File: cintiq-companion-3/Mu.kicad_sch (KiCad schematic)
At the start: 12 parts, among them J1 Conn_01x03_Pin

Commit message: updated notes
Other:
- note added: "rough HSIO plan: HSIO A: USB3, 2nd E-key PCIe x1 link and B-key PCIe x2/USB3 link 0: USB 3.2 Type-A 1: Wifi PCIe x1 link 2 2: B-key x2 Lane 1 / USB3.2 3: B-key x2 Lane 0 HSIO B: PCIe 4x1, HSIO11 sata/pcie with gpio for M-key m.2 slot 8: SSD PCIe x4 Lane 3 9: SSD PCIe x4 Lane 2 10: SSD PCIe x4 Lane 1 (/ SATA?) 11: SSD PCIe x4 Lane 0 / SATA HSIO C: PCIe 1x1 for E-key m.2 slot for Wifi 6: Wifi PCIe 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"
- note removed: "rough HSIO plan: HSIO A: USB3, 2nd E-key PCIe x1 link and B-key PCIe x2/USB3 link 0: USB 3.2 Type-A 1: Wifi PCIe x1 link 2 2: B-key x2 Lane 1/USB3.2 3: B-key x2 Lane 0 HSIO B: PCIe 4x1, HSIO11 sata/pcie with gpio for M-key m.2 slot 8: SSD PCIe x4 Lane 3 9: SSD PCIe x4 Lane 2 10: SSD PCIe x4 Lane 1 (/ SATA?) 11: SSD PCIe x4 Lane 0 / SATA HSIO C: PCIe 1x1 for E-key m.2 slot for Wifi 6: Wifi PCIe x1"
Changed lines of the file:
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@@
 		)
 	)
-	(text_box "USB2 P3/P4 used for 13HD stuff?"
-		(exclude_from_sim no)
-		(at 265.43 203.2 0)
-		(size 39.37 13.97)
+	(text_box "USB2 P3/P4 used for M.2 slots"
+		(exclude_from_sim no)
+		(at 264.16 198.12 0)
+		(size 40.64 10.16)
 		(stroke
 			(width 0)
@@
 		)
 	)
-	(text_box "USB2 P1/P2 used for USB3.0?"
-		(exclude_from_sim no)
-		(at 265.43 193.04 0)
-		(size 39.37 10.16)
+	(text_box "USB2 P1/P2 used for 13HD stuff"
+		(exclude_from_sim no)
+		(at 264.16 187.96 0)
+		(size 40.64 10.16)
+		(stroke
+			(width 0)
+			(type default)
+		)
+		(fill
+			(type none)
+		)
+		(effects
+			(font
+				(size 2.54 2.54)
+				(thickness 0.508)
+				(bold yes)
+				(color 255 121 154 1)
+			)
+			(justify left top)
+		)
+	)
+	(text_box "USB2 P7/P8 used for type-c + ?"
+		(exclude_from_sim no)
+		(at 264.16 208.28 0)
+		(size 40.64 10.16)
 		(stroke
 			(width 0)
@@
 		)
 	)
-	(text "rough HSIO plan:\n\nHSIO A:\nUSB3, 2nd E-key PCIe x1 link and B-key PCIe x2/USB3 link\n0:  USB 3.2 Type-A\n1:  Wifi PCIe x1 link 2\n2:  B-key x2 Lane 1/USB3.2\n3:  B-key x2 Lane 0\n\nHSIO B:\nPCIe 4x1, HSIO11 sata/pcie with gpio for M-key m.2 slot\n8:  SSD PCIe x4 Lane 3\n9:  SSD PCIe x4 Lane 2\n10: SSD PCIe x4 Lane 1 (/ SATA?)\n11: SSD PCIe x4 Lane 0 / SATA\n\nHSIO C:\nPCIe 1x1 for E-key m.2 slot for Wifi\n6:  Wifi PCIe x1 "
+	(text "rough HSIO plan:\n\nHSIO A:\nUSB3, 2nd E-key PCIe x1 link and B-key PCIe x2/USB3 link\n0:  USB 3.2 Type-A\n1:  Wifi PCIe x1 link 2\n2:  B-key x2 Lane 1 / USB3.2\n3:  B-key x2 Lane 0\n\nHSIO B:\nPCIe 4x1, HSIO11 sata/pcie with gpio for M-key m.2 slot\n8:  SSD PCIe x4 Lane 3\n9:  SSD PCIe x4 Lane 2\n10: SSD PCIe x4 Lane 1 (/ SATA?)\n11: SSD PCIe x4 Lane 0 / SATA\n\nHSIO C:\nPCIe 1x1 for E-key m.2 slot for Wifi\n6:  Wifi PCIe x1 "
 		(exclude_from_sim no)
 		(at 127 123.19 0)

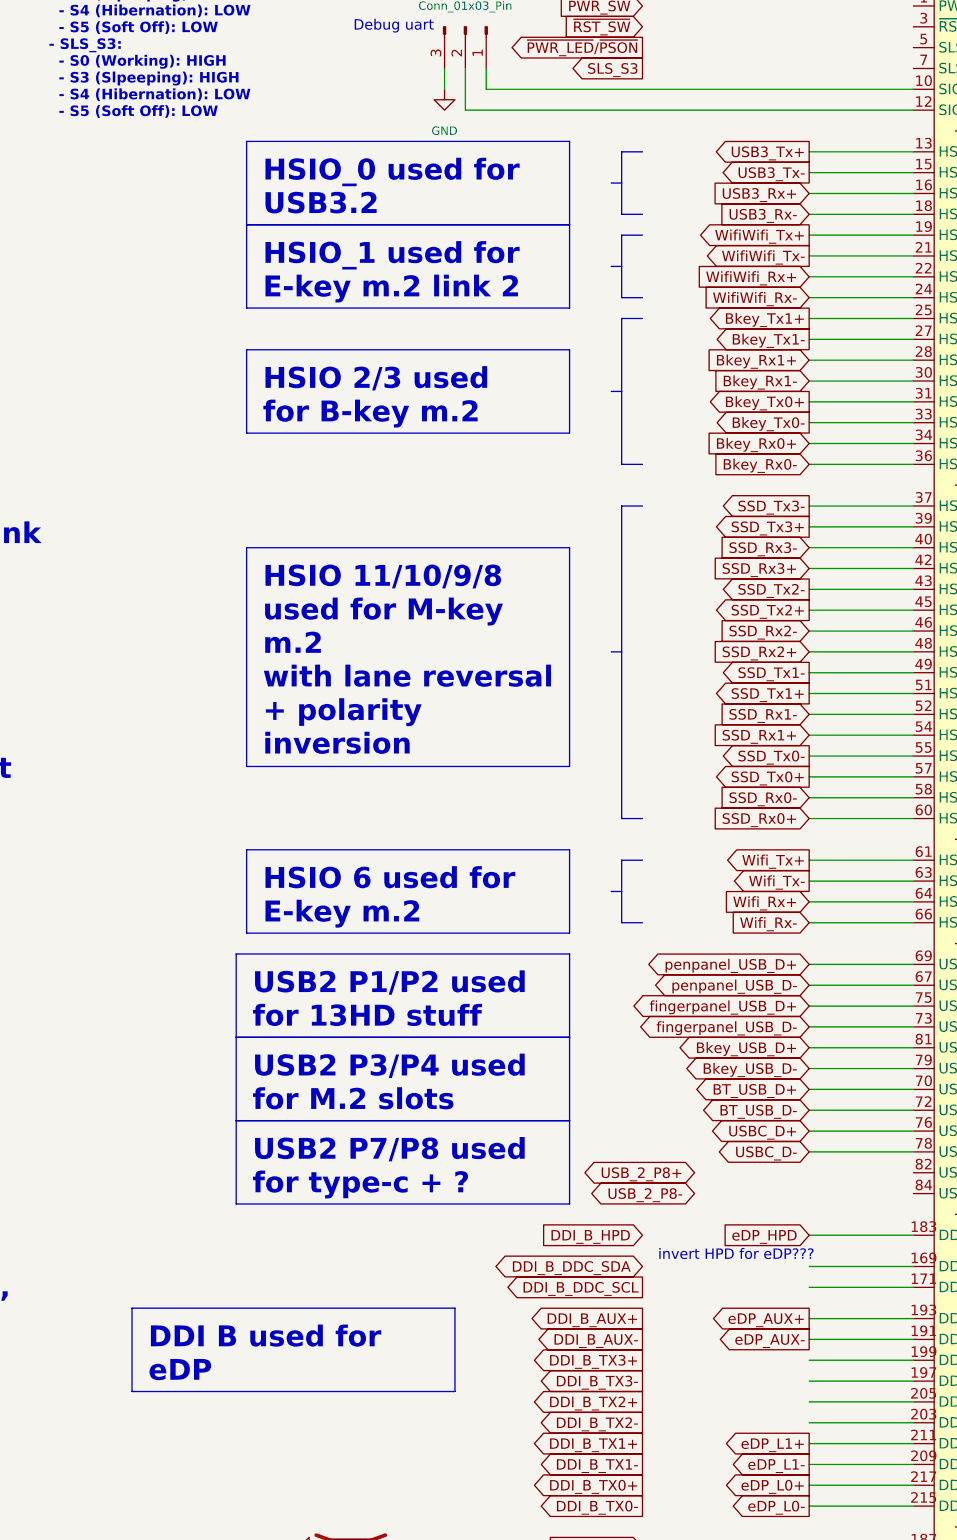
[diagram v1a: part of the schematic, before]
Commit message: unflipped m-key polarity for sata
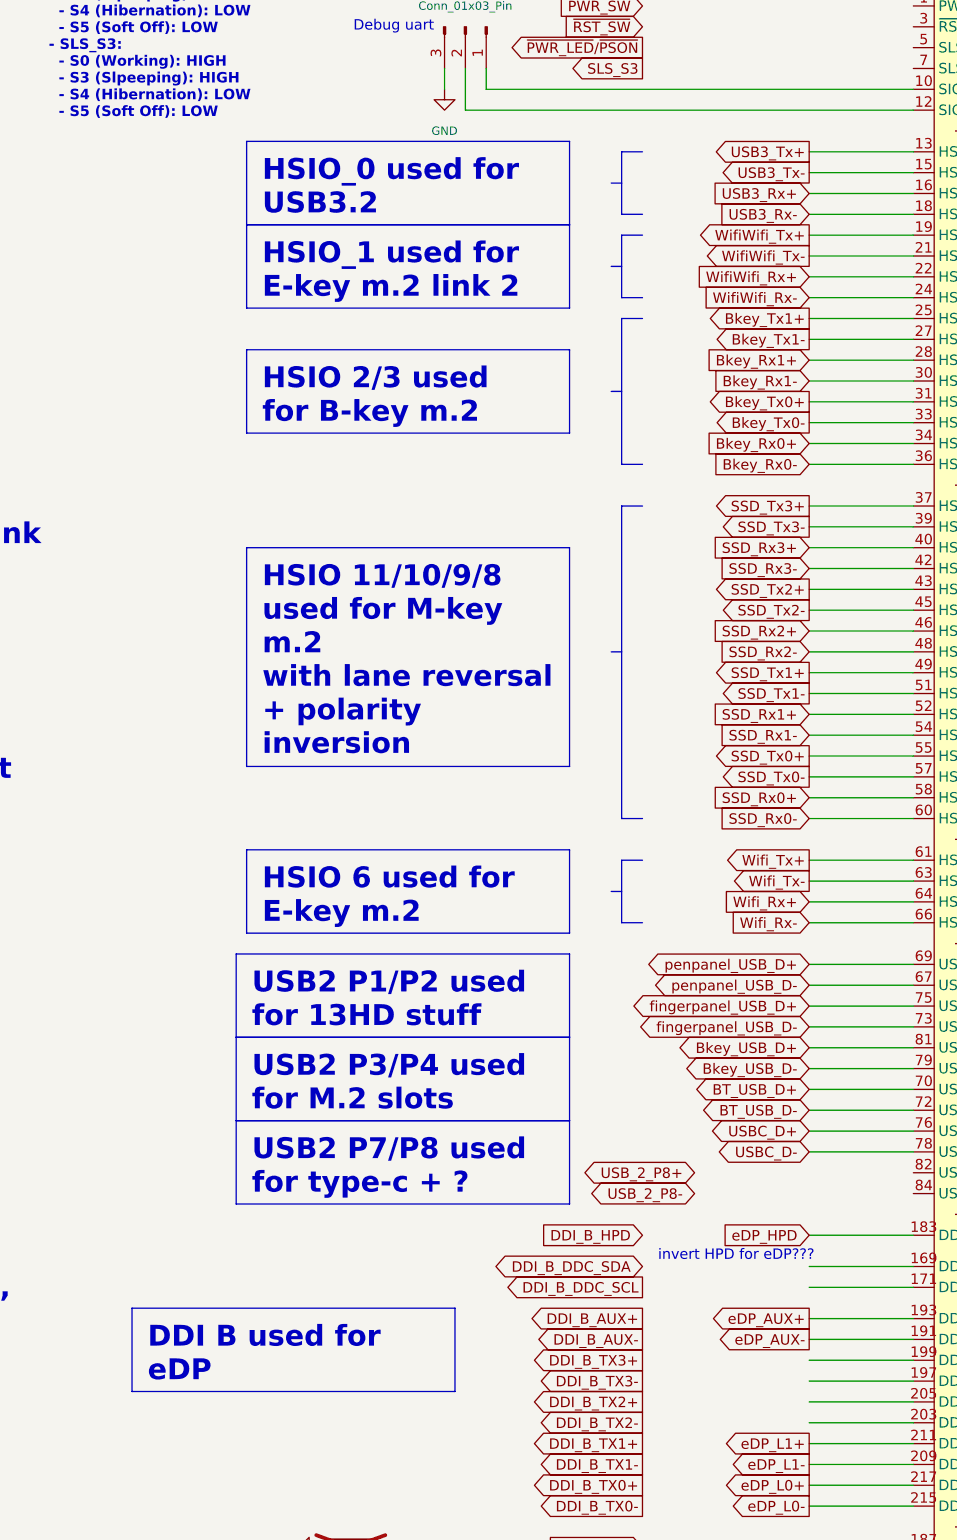
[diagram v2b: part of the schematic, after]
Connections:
- net SSD_Rx0+: now also A1.58 (HSIO11_RX+); no longer A1.60 (HSIO11_RX-)
- net SSD_Rx0-: now also A1.60 (HSIO11_RX-); no longer A1.58 (HSIO11_RX+)
- net SSD_Rx1+: now also A1.52 (HSIO10_RX+); no longer A1.54 (HSIO10_RX-)
- net SSD_Rx1-: now also A1.54 (HSIO10_RX-); no longer A1.52 (HSIO10_RX+)
- net SSD_Rx2+: now also A1.46 (HSIO9_RX+); no longer A1.48 (HSIO9_RX-)
- net SSD_Rx2-: now also A1.48 (HSIO9_RX-); no longer A1.46 (HSIO9_RX+)
- net SSD_Rx3+: now also A1.40 (HSIO8_RX+); no longer A1.42 (HSIO8_RX-)
- net SSD_Rx3-: now also A1.42 (HSIO8_RX-); no longer A1.40 (HSIO8_RX+)
- net SSD_Tx0+: now also A1.55 (HSIO11_TX+); no longer A1.57 (HSIO11_TX-)
- net SSD_Tx0-: now also A1.57 (HSIO11_TX-); no longer A1.55 (HSIO11_TX+)
- net SSD_Tx1+: now also A1.49 (HSIO10_TX+); no longer A1.51 (HSIO10_TX-)
- net SSD_Tx1-: now also A1.51 (HSIO10_TX-); no longer A1.49 (HSIO10_TX+)
- net SSD_Tx2+: now also A1.43 (HSIO9_TX+); no longer A1.45 (HSIO9_TX-)
- net SSD_Tx2-: now also A1.45 (HSIO9_TX-); no longer A1.43 (HSIO9_TX+)
- net SSD_Tx3+: now also A1.37 (HSIO8_TX+); no longer A1.39 (HSIO8_TX-)
- net SSD_Tx3-: now also A1.39 (HSIO8_TX-); no longer A1.37 (HSIO8_TX+)
